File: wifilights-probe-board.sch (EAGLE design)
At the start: 48 parts, among them Q1 BUK98180-100A, Q2 BUK98180-100A, Q3 BUK98180-100A, Q4 BUK98180-100A, U2 PCA9685

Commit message: Probe board complete
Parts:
- removed A, B: (no value), adafruit:PINHD-1X1
- removed B2: DBLS203G, rectifier:DBLS203G
- removed C3: 220pf, resistor:C-EUC0805K
- removed C4, C6: 0.1uF, resistor:C-EUC0805K
- removed C7: 10uF, resistor:C-EUC0805K
- removed D1: MBRS140T3, diode:MBRS130LT3
- removed L1: 220uf, SparkFun-Passives:INDUCTORSDR0403-560KL
- removed LED3: OVSTRGBBCR8, led:OVSTRGBBCR8
- removed MPU: ESP8266_ESP-12, ESP8266-ESP12:ESP8266_ESP-12
- removed PWR, THINKING: (no value), led:LEDCHIP-LED0805
- removed Q1, Q2, Q3, Q4: BUK98180-100A, nxp_60:BUK98180-100A
- removed R4: 1K, resistor:R-EU_R0805
- removed R5, R6: 1k, resistor:R-EU_R0805
- removed R7: ???, resistor:R-EU_R0805
- removed R8: 10K, resistor:R-EU_R0805
- removed REG1: MC33063/MC34063D, adafruit:MC33063/MC34063D
- removed REG2: MC33269-SO8, linear:MC33269-SO8
- removed TEMPERATURE: MPL3115A2LGA8, SparkFun-Sensors:MPL3115A2LGA8
- removed U$1, U$2, U$3: LUXEON-REBEL, SparkFun-LED:LUXEON-REBEL
- removed U2: PCA9685, adafruit:PCA9685
- added F1: 500mA, SparkFun:PTCSMD
- added H2, H3, H4, H5: SEW_HOLE, LilyPad-Wearables:SEW_HOLE
- added J1: 22-05-7028-02, con-molex:22-05-7028-02
- added JP1: (no value), SparkFun-Connectors:M05X2SHD
- added JP7: USB_MICROB_PLUGCONN-11752, SparkFun-Connectors:USB_MICROB_PLUGCONN-11752
- added S1: SWITCH-MOMENTARY-2PTH, SparkFun-Electromechanical:SWITCH-MOMENTARY-2PTH
- added TPCHPD, TPGPIO0, TPGPIO2, TPRX, TPTX: (no value), SparkFun-Connectors:M01POGOPIN_HOLE_0.58
- added U1: FT232R, SparkFun:FT232RLSSOP
- C1, C2: device resistor:C-EUC0805K -> SparkFun-Capacitors:0.1UF-25V(+80/-20%)(0603)
- LED1: value OVSTRGBBCR8 -> Red; device led:OVSTRGBBCR8 -> SparkFun-LED:LED-RED0603
- LED2: value OVSTRGBBCR8 -> Green; device led:OVSTRGBBCR8 -> SparkFun-LED:LED-GREEN0603
- P_RED, P_WHITE, RED, SCL, SDA, TP12V, TP3.3V, TP5V, TPGND, WHITE: value TEST-POINT3X5 -> (none); device SparkFun-Passives:TEST-POINT3X5 -> SparkFun-Connectors:M01POGOPIN_HOLE_0.58
- R1: value 220 ??? -> 330; device resistor:R-EU_R0805 -> SparkFun-Resistors:330OHM1/10W1%(0603)
- R2: value ??? -> 330; device resistor:R-EU_R0805 -> SparkFun-Resistors:330OHM1/10W1%(0603)
- R3: value 3K -> 1k; device resistor:R-EU_R0805 -> SparkFun-Passives:RESISTORAXIAL-0.3
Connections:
- removed net BLUE: Q2.G, U2.PWM1
- removed net COMP: R3.2, R4.1, REG1.COMP
- removed net GREEN: Q4.G, U2.PWM3
- removed net N$10: U$1.C, U$2.A
- removed net N$11: U$2.C, U$3.A
- removed net N$13: R1.2, REG1.DC, REG1.IPK, REG1.SWC
- removed net N$14: PWR.A, R2.2
- removed net N$15: R7.2, THINKING.A
- removed net N$16: C3.1, REG1.TC
- removed net N$17: C4.1, TEMPERATURE.CAP
- removed net N$18: A.1, B2.AC1
- removed net N$19: B.1, B2.AC2
- removed net N$20: R8.2, U2.#OE
- removed net N$25: MPU.GPIO14
- removed net N$26: MPU.GPIO16
- removed net N$27: MPU.CH_PD
- removed net N$28: MPU.ADC
- removed net N$29: MPU.REST
- removed net N$32: MPU.GPIO4
- removed net N$33: MPU.GPIO0
- removed net N$34: MPU.GPIO2
- removed net N$35: MPU.GPIO15
- removed net N$36: MPU.GPIO5
- removed net N$5: LED2-R.C, LED3-R.A
- removed net N$6: LED1-R.C, LED2-R.A
- removed net N$7: LED1G$1.C, LED2G$1.A
- removed net N$8: LED2G$1.C, LED3G$1.A
- removed net P_BLUE: LED3G$1.C, Q2.D
- removed net P_GREEN: LED3-G.C, Q4.D
- removed net RESET: MPU.TXD
- removed net SWE: D1.C, L1.2, REG1.SWE
- removed net THINKING: MPU.RXD, R7.1
- new net CTS: U1.CTS
- new net DCD: U1.DCD
- new net DSR: U1.DSR
- new net DTR: U1.DTR
- new net GPIO0: R3.1, S1.2, TPGPIO0.1
- new net N$3: F1.1, JP7.VCC
- new net PWREN: U1.PWREN
- new net RI: U1.RI
- new net RTS: U1.RTS
- new net RXD: TPRX.1, U1.RXD
- new net RXLED: LED2.C, U1.RXLED
- new net SLEEP: U1.SLEEP
- new net TXD: TPTX.1, U1.TXD
- new net TXDEN: U1.TXDEN
- new net TXLED: LED1.C, U1.TXLED
- new net USB_D+: JP7.D+, U1.USBDP
- new net USB_D-: JP7.D-, U1.USBDM
- new net VCC: C2.1, C5.+, F1.2, U1.VCC
- net 12V: now also J1-1.S; no longer B2.+, LED1-G.A, LED1-R.A, LED1G$1.A, R1.1, REG1.VCC, U$1.A
- net 3.3V: now also JP1.2, R1.2, R2.2, R3.2, TPCHPD.1, TPGPIO2.1, U1.3V3OUT, U1.VCCIO; no longer C2.1, C7.1, MPU.VCC, R2.1, R5.2, R6.2, REG2.OUT, REG2.OUT@1, REG2.OUT@2, REG2.OUT@3, TEMPERATURE.VDD, TEMPERATURE.VDDIO, U2.VDD
- net 5V: now also JP1.1; no longer C5.+, C6.1, L1.1, R3.1, REG2.IN
- net GND: now also H2.P$1, H3.P$1, H4.P$1, H5.P$1, J1-2.S, JP1.10, JP1.9, JP7.GND, S1.1, U1.AGND, U1.GND18, U1.GND21, U1.GND7, U1.TEST; no longer B2.-, C3.2, C4.2, C6.2, C7.2, D1.A, MPU.GND, PWR.C, Q1.S, Q2.S, Q3.S, Q4.S, R4.2, R8.1, REG1.GND, REG2.GND/ADJ, TEMPERATURE.GND, THINKING.C, U$1.S, U$2.S, U$3.S, U2.EXTCLK, U2.GND
- net N$1: now also LED1.A, R1.1; no longer LED1-G.C, LED2-G.A
- net N$2: now also LED2.A, R2.1; no longer LED2-G.C, LED3-G.A
- net P_RED: now also JP1.8; no longer LED3-R.C, Q3.D
- net P_WHITE: now also JP1.6; no longer Q1.D, U$3.C
- net RED: now also JP1.7; no longer Q3.G, U2.PWM2
- net SCL: now also JP1.3; no longer MPU.GPIO13, R6.1, TEMPERATURE.SDA, U2.SCL
- net SDA: now also JP1.4; no longer MPU.GPIO12, R5.1, TEMPERATURE.SCL, U2.SDA
- net WHITE: now also JP1.5; no longer Q1.G, U2.PWM0
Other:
- note added: "Note: The internal regulator can only source 50mA when running at 3.3V. Keep this in mind when attempting to power 3.3V devices off of the 3.3V pin."
- moved on the sheet: C1, C2, C5, H1

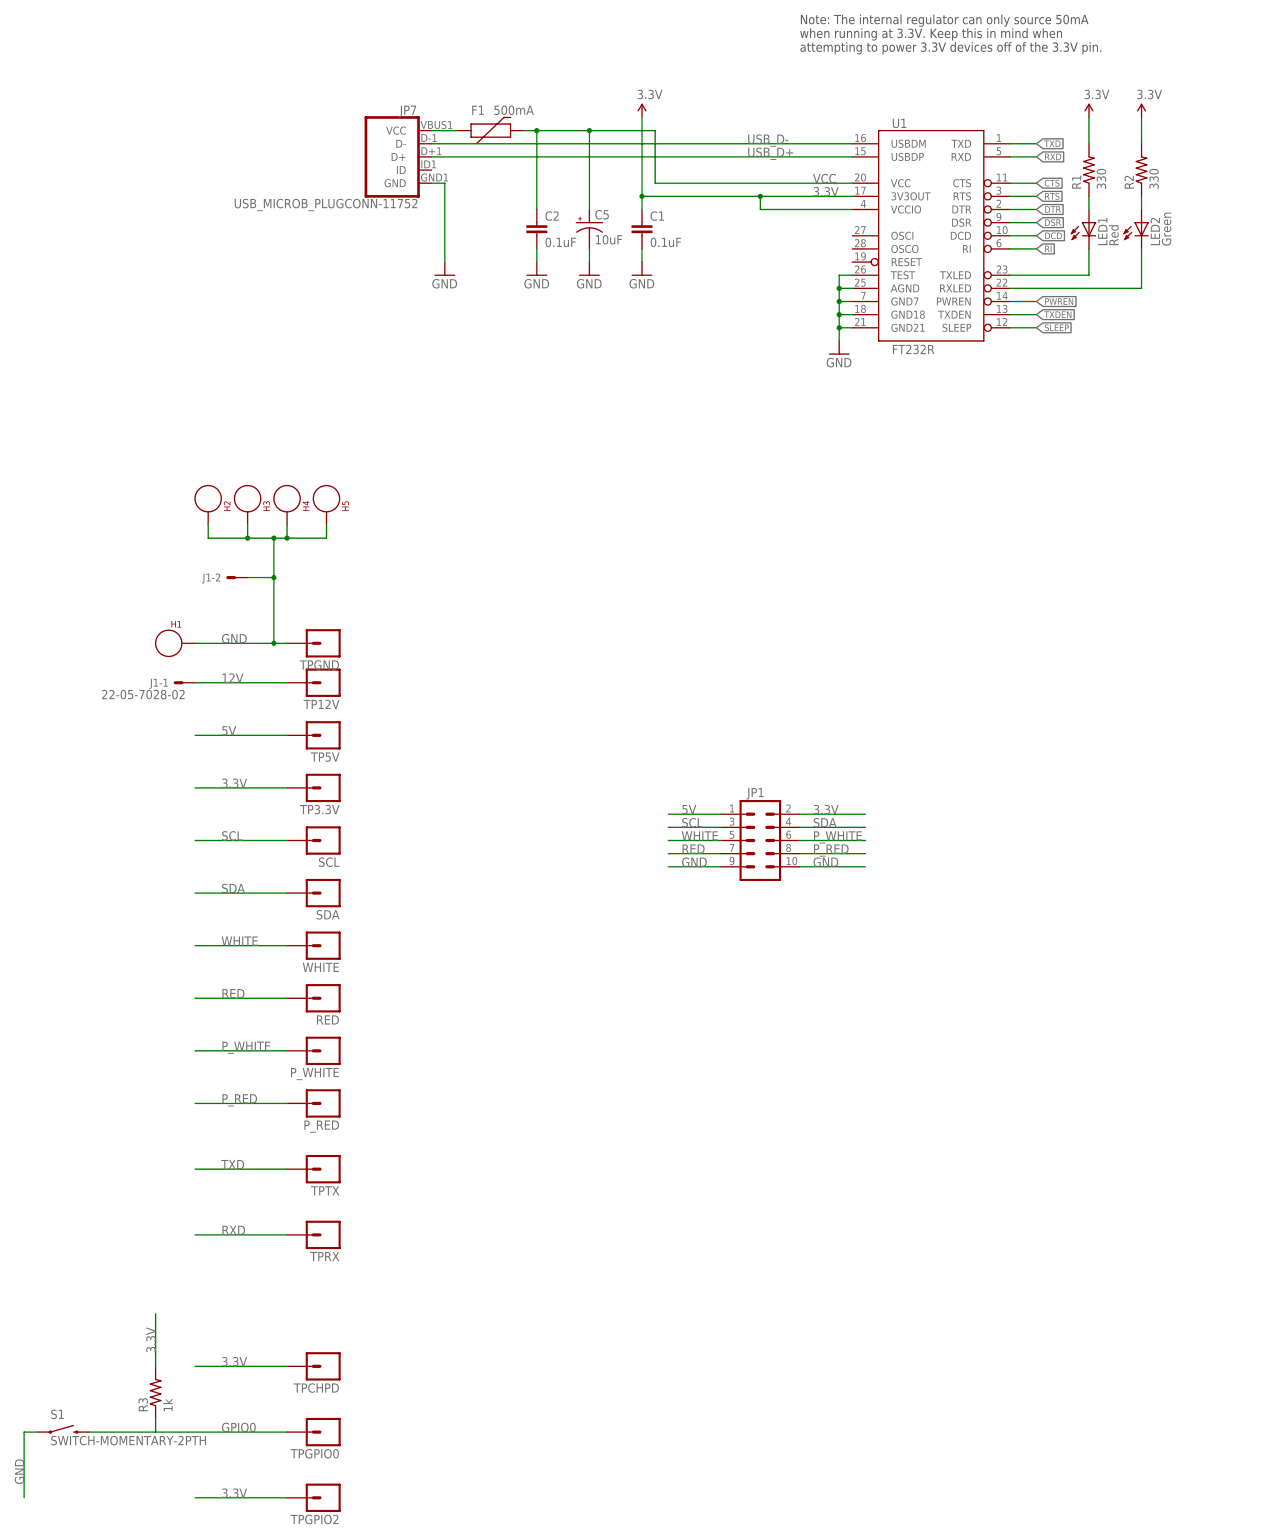
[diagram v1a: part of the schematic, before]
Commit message: Better probe board
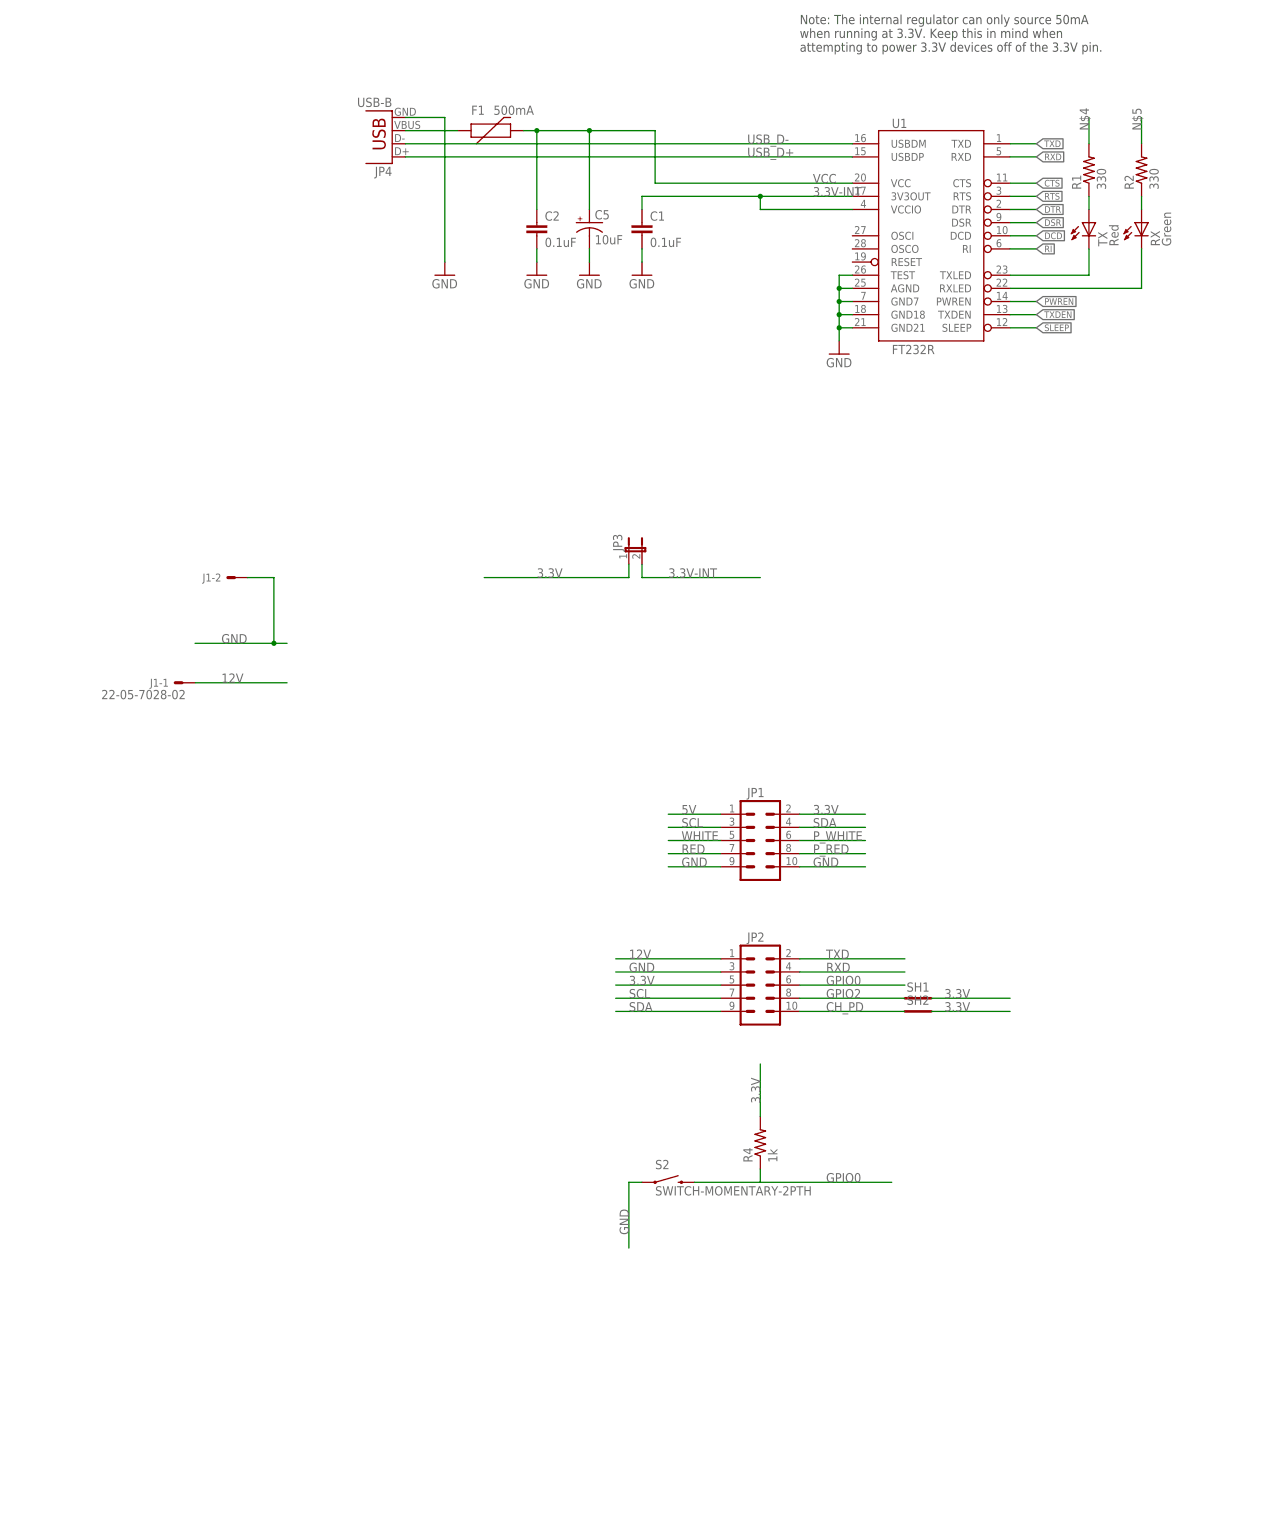
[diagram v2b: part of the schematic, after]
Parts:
- removed H1, H2, H3, H4, H5: SEW_HOLE, LilyPad-Wearables:SEW_HOLE
- removed JP7: USB_MICROB_PLUGCONN-11752, SparkFun-Connectors:USB_MICROB_PLUGCONN-11752
- removed P_RED, P_WHITE, RED, SCL, SDA, TP12V, TP3.3V, TP5V, TPCHPD, TPGND, TPGPIO0, TPGPIO2, TPRX, TPTX, WHITE: (no value), SparkFun-Connectors:M01POGOPIN_HOLE_0.58
- removed R3: 1k, SparkFun-Passives:RESISTORAXIAL-0.3
- removed S1: SWITCH-MOMENTARY-2PTH, SparkFun-Electromechanical:SWITCH-MOMENTARY-2PTH
- added JP2: (no value), SparkFun-Connectors:M05X2SHD_LOCK
- added JP3: (no value), SparkFun-Retired:JUMPER-2PTH
- added JP4: USB-B, SparkFun-Connectors:USBPTH
- added R4: 1k, SparkFun-Passives:RESISTORAXIAL-0.3
- added S2: SWITCH-MOMENTARY-2PTH, SparkFun-Electromechanical:SWITCH-MOMENTARY-2PTH
- added SH1, SH2: SHORT-HT5, shorts-old:SHORT-HT5
- renumbered LED1 to TX, LED2 to RX
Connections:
- new net 3.3V-INT: C1.1, JP3.2, U1.3V3OUT, U1.VCCIO
- new net CH_PD: JP2.10, SH2.P$1
- new net GPIO2: JP2.8, SH1.P$1
- new net N$4: R1.2
- new net N$5: R2.2
- net 12V: now also JP2.1; no longer TP12V.1
- net 3.3V: now also JP2.5, JP3.1, R4.2, SH1.P$2, SH2.P$2; no longer C1.1, R1.2, R2.2, R3.2, TP3.3V.1, TPCHPD.1, TPGPIO2.1, U1.3V3OUT, U1.VCCIO
- net 5V: no longer TP5V.1
- net GND: now also JP2.3, JP4.GND, S2.1; no longer H1.P$1, H2.P$1, H3.P$1, H4.P$1, H5.P$1, JP7.GND, S1.1, TPGND.1
- net GPIO0: now also JP2.6, R4.1, S2.2; no longer R3.1, S1.2, TPGPIO0.1
- net N$3: now also JP4.VBUS; no longer JP7.VCC
- net P_RED: no longer P_RED.1
- net P_WHITE: no longer P_WHITE.1
- net RED: no longer RED.1
- net RXD: now also JP2.4; no longer TPRX.1
- net SCL: now also JP2.7; no longer SCL.1
- net SDA: now also JP2.9; no longer SDA.1
- net TXD: now also JP2.2; no longer TPTX.1
- net USB_D+: now also JP4.D+; no longer JP7.D+
- net USB_D-: now also JP4.D-; no longer JP7.D-
- net WHITE: no longer WHITE.1

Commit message: Mk6 complete & DRC'd
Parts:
- removed J1: 22-05-7028-02, con-molex:22-05-7028-02
- removed JP2: (no value), SparkFun-Connectors:M05X2SHD_LOCK
- removed JP3: (no value), SparkFun-Retired:JUMPER-2PTH
- removed JP4: USB-B, SparkFun-Connectors:USBPTH
- removed R4: 1k, SparkFun-Passives:RESISTORAXIAL-0.3
- removed S2: SWITCH-MOMENTARY-2PTH, SparkFun-Electromechanical:SWITCH-MOMENTARY-2PTH
- removed SH1, SH2: SHORT-HT5, shorts-old:SHORT-HT5
- added CN1: (no value), adafruit:USBMINIB
- added PROGRAM: (no value), SparkFun-Electromechanical:SWITCH-SPDT-SMD-A
- added RESET: SWITCH-MOMENTARY-2PTH, SparkFun-Electromechanical:SWITCH-MOMENTARY-2PTH
- added X1: 53261-06, con-molex:53261-06
- C1, C2: device SparkFun-Capacitors:0.1UF-25V(+80/-20%)(0603) -> SparkFun-Passives:CAP1206
- JP1: value (none) -> 12V DC; device SparkFun-Connectors:M05X2SHD -> SparkFun-Connectors:M02JST-PTH-VERT
- R1, R2: device SparkFun-Resistors:330OHM1/10W1%(0603) -> SparkFun-Passives:RESISTOR1206
- RX: value Green -> GREEN; device SparkFun-LED:LED-GREEN0603 -> SparkFun-LED:LED1206
- TX: value Red -> RED; device SparkFun-LED:LED-RED0603 -> SparkFun-LED:LED1206
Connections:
- removed net 3.3V-INT: C1.1, JP3.2, U1.3V3OUT, U1.VCCIO
- removed net 5V: JP1.1
- removed net CH_PD: JP2.10, SH2.P$1
- removed net GPIO0: JP2.6, R4.1, S2.2
- removed net GPIO2: JP2.8, SH1.P$1
- removed net N$4: R1.2
- removed net N$5: R2.2
- removed net P_RED: JP1.8
- removed net P_WHITE: JP1.6
- removed net RED: JP1.7
- removed net SCL: JP1.3, JP2.7
- removed net SDA: JP1.4, JP2.9
- removed net WHITE: JP1.5
- net 12V: now also JP1.2, X1-6.S; no longer J1-1.S, JP2.1
- net 3.3V: now also C1.1, R1.2, R2.2, U1.3V3OUT, U1.VCCIO; no longer JP1.2, JP2.5, JP3.1, R4.2, SH1.P$2, SH2.P$2
- net DTR: now also PROGRAM.P, X1-4.S
- net GND: now also CN1.GND, JP1.1, PROGRAM.S, RESET.2, X1-5.S; no longer J1-2.S, JP1.10, JP1.9, JP2.3, JP4.GND, S2.1
- net N$3: now also CN1.VBUS; no longer JP4.VBUS
- net RTS: now also RESET.1, X1-3.S
- net RXD: now also X1-2.S; no longer JP2.4
- net TXD: now also X1-1.S; no longer JP2.2
- net USB_D+: now also CN1.D+; no longer JP4.D+
- net USB_D-: now also CN1.D-; no longer JP4.D-
